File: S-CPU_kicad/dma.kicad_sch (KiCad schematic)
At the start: 115 parts

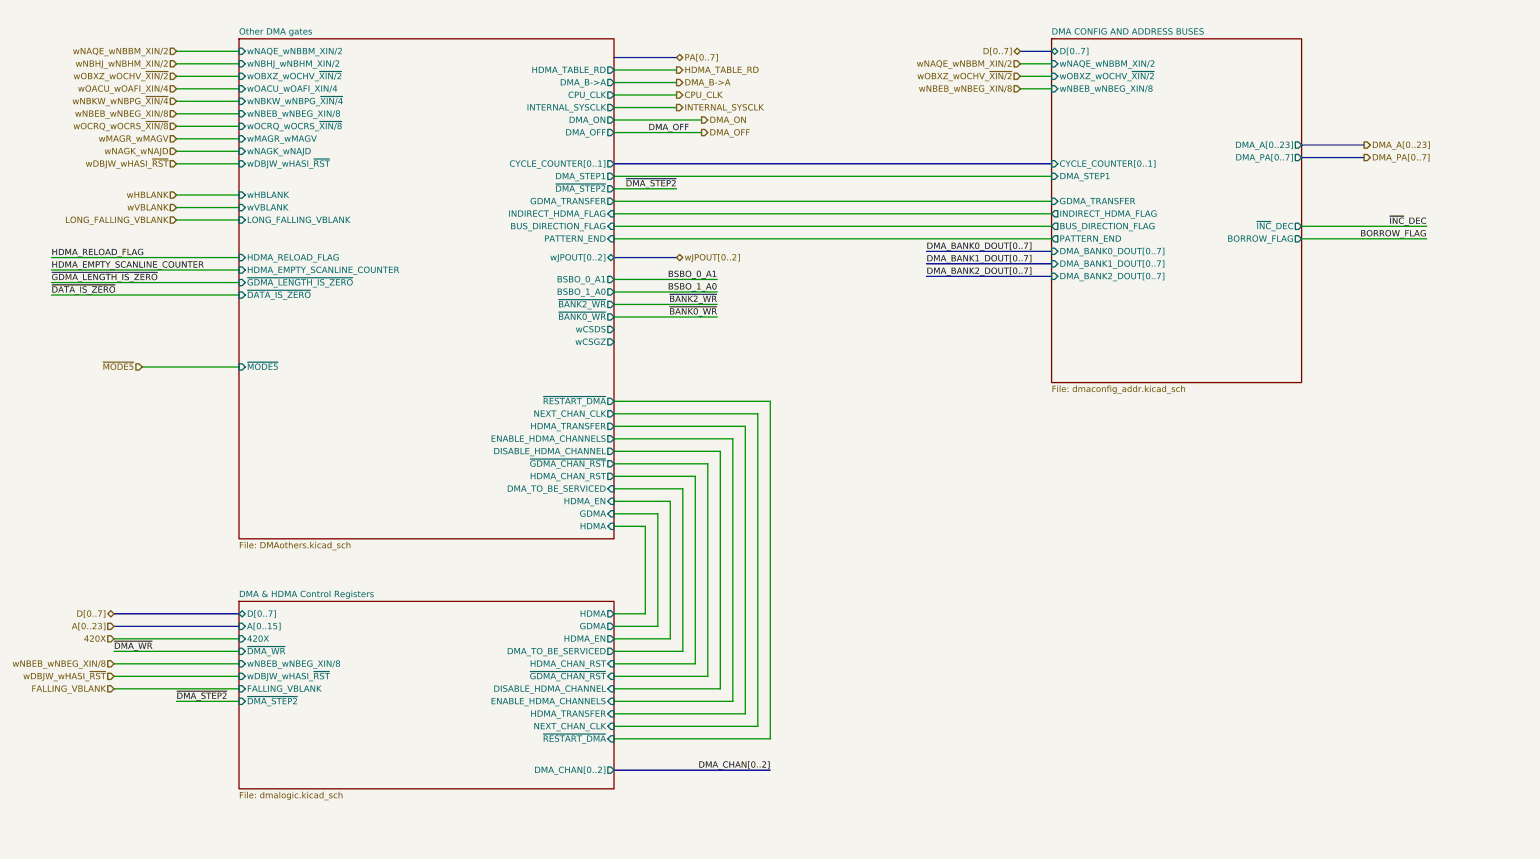
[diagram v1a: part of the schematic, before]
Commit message: Further tidying of the DMA section. New sheet added dedicated to GDMA/ HDMA Start and Stop signals.
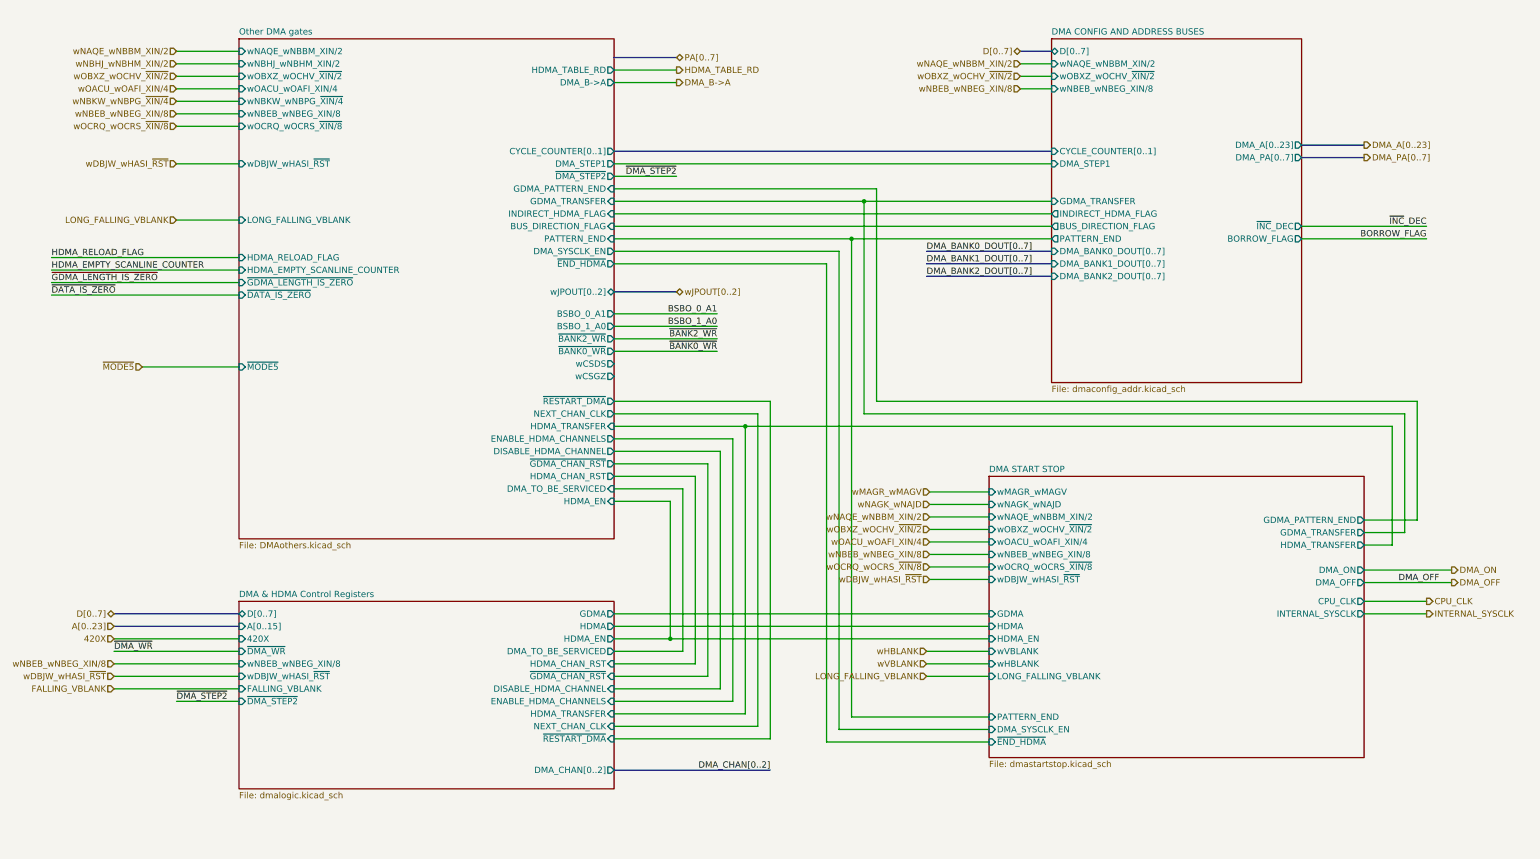
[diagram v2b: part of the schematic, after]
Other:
- added sheet DMA START STOP (dmastartstop.kicad_sch)
- sheet Other DMA gates ports: added DMA_SYSCLK_EN, GDMA_PATTERN_END, ~{END_HDMA}; removed CPU_CLK, DMA_OFF, DMA_ON, GDMA, HDMA, INTERNAL_SYSCLK, wHBLANK, wMAGR_wMAGV, wNAGK_wNAJD, wVBLANK

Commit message: General update a
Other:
- sheet DMA & HDMA Control Registers ports: added ~{DMA_CHAN_RST}; removed ~{GDMA_CHAN_RST}
- sheet DMA START STOP ports: added HDMA_ON; removed none
- sheet Other DMA gates ports: added DMA_ON, HDMA_ON, PA[0..7], ~{DMA_CHAN_RST}; removed ~{GDMA_CHAN_RST}
- note added: "DMA Registers Parameters for DMA Transfer B Address A Address (Low Byte) A Address (High Byte) A Address Bank Number Bytes to Transfer (Low Byte) (DMA) Number Bytes to Transfer (High Byte) (DMA) Data Bank (H-DMA) A2 Table Address (Low Byte) A2 Table Address (High Byte) Number of Lines to Transfer (HDMA) Fast Access memory x x x Fast Access memory mirror"
- note removed: "DMA Registers Parameters for DMA Transfer B Address A Address (Low Byte) A Address (High Byte) A Address Bank Number Bytes to Transfer (Low Byte) (DMA) Number Bytes to Transfer (High Byte) (DMA) Data Bank (H-DMA) A2 Table Address (Low Byte) A2 Table Address (High Byte) Number of Lines to Transfer (H-DMA) Fast Access memory x x x Fast Access memory mirror"
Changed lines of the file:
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@@
   (junction (at 357.505 269.24) (diameter 0) (color 0 0 0 0)
   )
+  (junction (at 783.59 273.05) (diameter 0) (color 0 0 0 0)
+  )
   (junction (at 487.045 116.84) (diameter 0) (color 0 0 0 0)
   )
@@
     (stroke (width 0) (type default))
   )
+  (wire (pts (xy 662.94 213.36) (xy 662.94 246.38))
+    (stroke (width 0) (type default))
+  )
   (wire (pts (xy 360.045 216.535) (xy 360.045 184.785))
     (stroke (width 0) (type default))
@@
     (stroke (width 0) (type default))
   )
+  (wire (pts (xy 660.4 215.9) (xy 660.4 248.92))
+    (stroke (width 0) (type default))
+  )
   (wire (pts (xy 259.08 220.98) (xy 266.065 220.98))
     (stroke (width 0) (type default))
@@
     (stroke (width 0) (type default))
   )
-  (wire (pts (xy 782.955 241.3) (xy 782.955 265.43))
+  (wire (pts (xy 788.67 241.3) (xy 788.67 265.43))
     (stroke (width 0) (type default))
   )
@@
     (stroke (width 0) (type default))
   )
+  (wire (pts (xy 781.05 248.92) (xy 781.05 270.51))
+    (stroke (width 0) (type default))
+  )
   (polyline (pts (xy 600.075 348.615) (xy 553.085 348.615))
     (stroke (width 0) (type default))
@@
     (stroke (width 0) (type default))
   )
+  (wire (pts (xy 783.59 246.38) (xy 783.59 273.05))
+    (stroke (width 0) (type default))
+  )
   (bus (pts (xy 685.8 208.28) (xy 711.2 208.28))
     (stroke (width 0) (type default))
@@
     (stroke (width 0) (type default))
   )
-  (wire (pts (xy 774.7 273.05) (xy 792.48 273.05))
-    (stroke (width 0) (type default))
-  )
   (wire (pts (xy 240.665 419.735) (xy 257.81 419.735))
     (stroke (width 0) (type default))
@@
     (stroke (width 0) (type default))
   )
-  (bus (pts (xy 622.3 216.535) (xy 635 216.535))
+  (bus (pts (xy 622.3 176.53) (xy 635 176.53))
     (stroke (width 0) (type default))
   )
@@
     (stroke (width 0) (type default))
   )
-  (wire (pts (xy 782.955 265.43) (xy 774.7 265.43))
+  (wire (pts (xy 788.67 265.43) (xy 774.7 265.43))
     (stroke (width 0) (type default))
   )
@@
     (stroke (width 0) (type default))
   )
+  (wire (pts (xy 622.3 233.68) (xy 632.46 233.68))
+    (stroke (width 0) (type default))
+  )
   (wire (pts (xy 541.655 548.005) (xy 558.165 548.005))
     (stroke (width 0) (type default))
@@
     (stroke (width 0) (type default))
   )
-  (wire (pts (xy 780.415 243.84) (xy 780.415 267.97))
+  (wire (pts (xy 786.13 243.84) (xy 786.13 267.97))
     (stroke (width 0) (type default))
   )
@@
     (stroke (width 0) (type default))
   )
+  (wire (pts (xy 774.7 273.05) (xy 783.59 273.05))
+    (stroke (width 0) (type default))
+  )
   (wire (pts (xy 156.845 422.275) (xy 227.965 422.275))
     (stroke (width 0) (type default))
@@
     (stroke (width 0) (type default))
   )
+  (wire (pts (xy 774.7 270.51) (xy 781.05 270.51))
+    (stroke (width 0) (type default))
+  )
   (wire (pts (xy 686.435 272.415) (xy 698.5 272.415))
     (stroke (width 0) (type default))
@@
     (stroke (width 0) (type default))
   )
-  (wire (pts (xy 648.97 243.84) (xy 780.415 243.84))
+  (wire (pts (xy 648.97 243.84) (xy 786.13 243.84))
     (stroke (width 0) (type default))
   )
@@
     (stroke (width 0) (type default))
   )
+  (wire (pts (xy 622.3 213.36) (xy 662.94 213.36))
+    (stroke (width 0) (type default))
+  )
   (wire (pts (xy 259.08 203.2) (xy 259.08 220.98))
     (stroke (width 0) (type default))
@@
     (stroke (width 0) (type default))
   )
-  (wire (pts (xy 785.495 262.89) (xy 774.7 262.89))
+  (wire (pts (xy 791.21 262.89) (xy 774.7 262.89))
     (stroke (width 0) (type default))
   )
@@
     (stroke (width 0) (type default))
   )
+  (wire (pts (xy 660.4 248.92) (xy 781.05 248.92))
+    (stroke (width 0) (type default))
+  )
   (wire (pts (xy 521.335 521.335) (xy 526.415 521.335))
     (stroke (width 0) (type default))
@@
     (stroke (width 0) (type default))
   )
-  (wire (pts (xy 675.64 238.76) (xy 785.495 238.76))
+  (wire (pts (xy 675.64 238.76) (xy 791.21 238.76))
     (stroke (width 0) (type default))
   )
@@
     (stroke (width 0) (type default))
   )
-  (wire (pts (xy 641.35 251.46) (xy 622.3 251.46))
+  (wire (pts (xy 622.3 251.46) (xy 641.35 251.46))
     (stroke (width 0) (type default))
   )
@@
     (stroke (width 0) (type default))
   )
-  (wire (pts (xy 780.415 267.97) (xy 774.7 267.97))
+  (wire (pts (xy 786.13 267.97) (xy 774.7 267.97))
     (stroke (width 0) (type default))
   )
@@
     (stroke (width 0) (type default))
   )
-  (wire (pts (xy 673.1 241.3) (xy 782.955 241.3))
+  (wire (pts (xy 673.1 241.3) (xy 788.67 241.3))
     (stroke (width 0) (type default))
   )
@@
     (stroke (width 0) (type default))
   )
+  (wire (pts (xy 662.94 246.38) (xy 783.59 246.38))
+    (stroke (width 0) (type default))
+  )
   (wire (pts (xy 83.82 495.3) (xy 93.345 495.3))
     (stroke (width 0) (type default))
@@
     (stroke (width 0) (type default))
   )
-  (wire (pts (xy 785.495 238.76) (xy 785.495 262.89))
+  (wire (pts (xy 791.21 238.76) (xy 791.21 262.89))
     (stroke (width 0) (type default))
   )
@@
     (stroke (width 0) (type default))
   )
+  (wire (pts (xy 783.59 273.05) (xy 792.48 273.05))
+    (stroke (width 0) (type default))
+  )
   (wire (pts (xy 261.62 289.56) (xy 266.065 289.56))
     (stroke (width 0) (type default))
@@
     (stroke (width 0) (type default))
   )
+  (wire (pts (xy 622.3 215.9) (xy 660.4 215.9))
+    (stroke (width 0) (type default))
+  )
   (wire (pts (xy 638.81 254) (xy 638.81 292.1))
     (stroke (width 0) (type default))
@@
     (stroke (width 0) (type default))
   )
+  (wire (pts (xy 632.46 231.14) (xy 622.3 231.14))
+    (stroke (width 0) (type default))
+  )
   (wire (pts (xy 362.585 445.135) (xy 356.87 445.135))
     (stroke (width 0) (type default))
@@
     (effects (font (size 1.27 1.27)) (justify left bottom))
   )
-  (text "DMA Registers\n\nParameters for DMA Transfer\nB Address\nA Address (Low Byte)\nA Address (High Byte)\nA Address Bank\nNumber Bytes to Transfer (Low Byte) (DMA)\nNumber Bytes to Transfer (High Byte) (DMA)\nData Bank (H-DMA)\nA2 Table Address (Low Byte)\nA2 Table Address (High Byte)\nNumber of Lines to Transfer (H-DMA) \nFast Access memory\nx\nx\nx\nFast Access memory mirror"
+  (text "DMA Registers\n\nParameters for DMA Transfer\nB Address\nA Address (Low Byte)\nA Address (High Byte)\nA Address Bank\nNumber Bytes to Transfer (Low Byte) (DMA)\nNumber Bytes to Transfer (High Byte) (DMA)\nData Bank (H-DMA)\nA2 Table Address (Low Byte)\nA2 Table Address (High Byte)\nNumber of Lines to Transfer (HDMA) \nFast Access memory\nx\nx\nx\nFast Access memory mirror"
     (at 554.355 387.985 0)
     (effects (font (size 1.27 1.27)) (justify left bottom))
@@
     (effects (font (size 1.27 1.27)) (justify right bottom))
   )
+  (label "wCSDS" (at 632.46 231.14 180) (fields_autoplaced)
+    (effects (font (size 1.27 1.27)) (justify right bottom))
+  )
   (label "DMA_BANK0_DOUT7" (at 237.49 205.74 0) (fields_autoplaced)
     (effects (font (size 1.27 1.27)) (justify left bottom))
@@
     (effects (font (size 1.27 1.27)) (justify right bottom))
   )
+  (label "wCSGZ" (at 632.46 233.68 180) (fields_autoplaced)
+    (effects (font (size 1.27 1.27)) (justify right bottom))
+  )
   (label "DMA_BANK0_DOUT3" (at 551.815 446.405 180) (fields_autoplaced)
     (effects (font (size 1.27 1.27)) (justify right bottom))
@@
     (effects (font (size 1.27 1.27)) (justify right))
   )
-  (hierarchical_label "wJPOUT[0..2]" (shape tri_state) (at 635 216.535 0) (fields_autoplaced)
+  (hierarchical_label "wJPOUT[0..2]" (shape tri_state) (at 635 176.53 0) (fields_autoplaced)
     (effects (font (size 1.27 1.27)) (justify left))
   )
@@
       (effects (font (size 1.27 1.27)) (justify right))
     )
-    (pin "~{GDMA_CHAN_RST}" input (at 622.3 294.64 0)
+    (pin "~{DMA_CHAN_RST}" input (at 622.3 294.64 0)
       (effects (font (size 1.27 1.27)) (justify right))
     )
@@
       (effects (font (size 1.27 1.27)) (justify right))
     )
-    (pin "~{GDMA_CHAN_RST}" output (at 622.3 251.46 0)
+    (pin "~{DMA_CHAN_RST}" output (at 622.3 251.46 0)
       (effects (font (size 1.27 1.27)) (justify right))
     )
@@
       (effects (font (size 1.27 1.27)) (justify right))
     )
-    (pin "wJPOUT[0..2]" tri_state (at 622.3 216.535 0)
+    (pin "wJPOUT[0..2]" tri_state (at 622.3 176.53 0)
       (effects (font (size 1.27 1.27)) (justify right))
     )
@@
       (effects (font (size 1.27 1.27)) (justify right))
     )
+    (pin "PA[0..7]" tri_state (at 622.3 168.91 0)
+      (effects (font (size 1.27 1.27)) (justify right))
+    )
+    (pin "DMA_ON" input (at 622.3 213.36 0)
+      (effects (font (size 1.27 1.27)) (justify right))
+    )
+    (pin "HDMA_ON" input (at 622.3 215.9 0)
+      (effects (font (size 1.27 1.27)) (justify right))
+    )
     (instances
       (project "S-CPU"
@@
       (effects (font (size 1.27 1.27)) (justify right))
     )
+    (pin "HDMA_ON" output (at 774.7 270.51 0)
+      (effects (font (size 1.27 1.27)) (justify right))
+    )

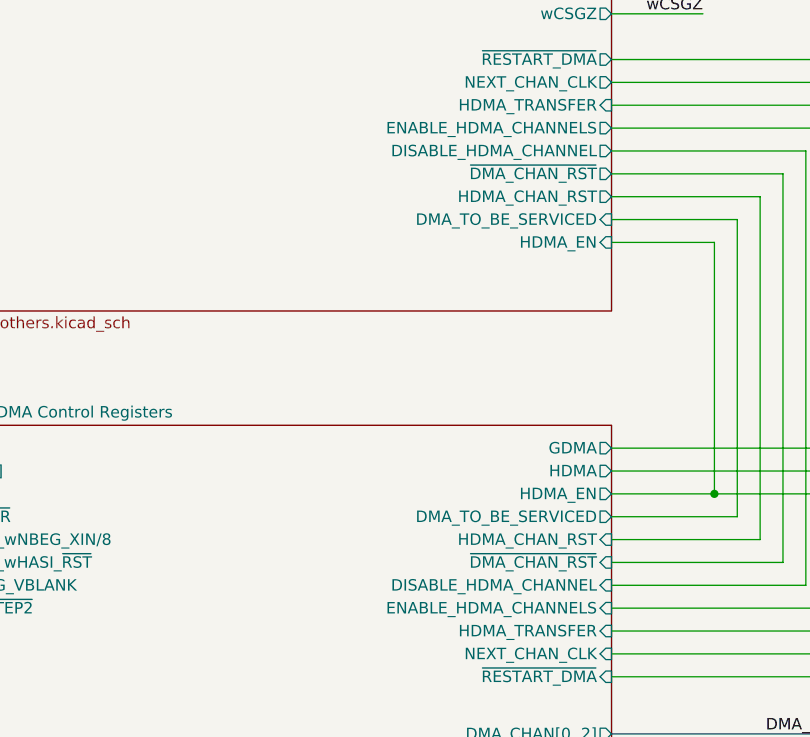
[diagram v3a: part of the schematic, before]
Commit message: HDMA section seems correct after all. More notes added.
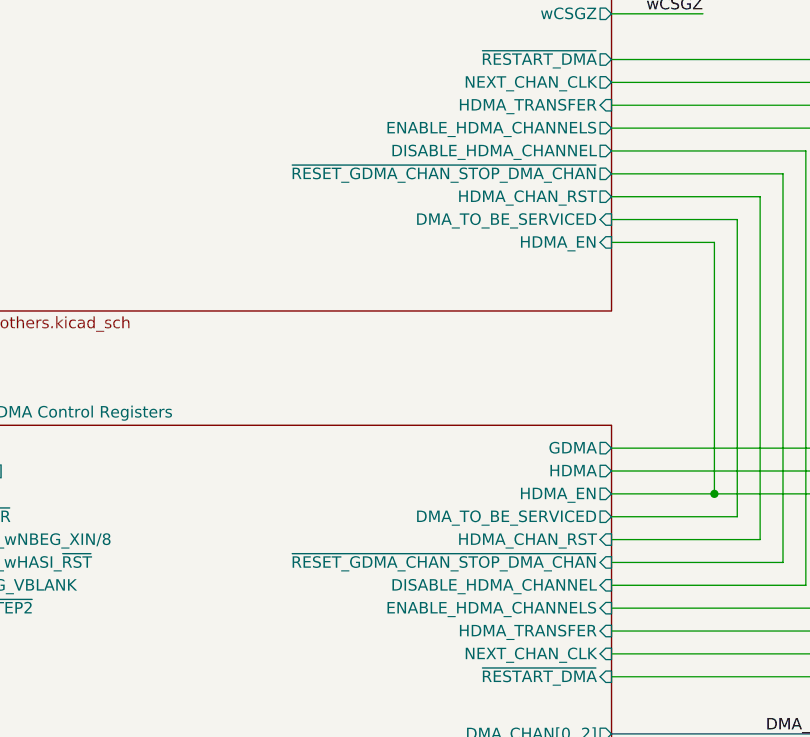
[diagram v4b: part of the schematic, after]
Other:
- sheet DMA & HDMA Control Registers ports: added ~{RESET_GDMA_CHAN_STOP_DMA_CHAN}; removed ~{DMA_CHAN_RST}
- sheet Other DMA gates ports: added ~{RESET_GDMA_CHAN_STOP_DMA_CHAN}; removed ~{DMA_CHAN_RST}
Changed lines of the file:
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@@
       (effects (font (size 1.27 1.27)) (justify right))
     )
-    (pin "~{DMA_CHAN_RST}" input (at 622.3 294.64 0)
+    (pin "~{RESET_GDMA_CHAN_STOP_DMA_CHAN}" input (at 622.3 294.64 0)
       (effects (font (size 1.27 1.27)) (justify right))
     )
@@
       (effects (font (size 1.27 1.27)) (justify right))
     )
-    (pin "~{DMA_CHAN_RST}" output (at 622.3 251.46 0)
+    (pin "~{RESET_GDMA_CHAN_STOP_DMA_CHAN}" output (at 622.3 251.46 0)
       (effects (font (size 1.27 1.27)) (justify right))
     )

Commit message: More DMA updates - extra notes regarding behaviour
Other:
- note added: "Latched on cycle 7 to 0 transition"
- note added: "Valid on cycle 0-1 and 4-5"
- moved on the sheet: OMNN
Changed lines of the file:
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@@
   (junction (at 261.62 236.22) (diameter 0) (color 0 0 0 0)
   )
+  (junction (at 351.79 512.445) (diameter 0) (color 0 0 0 0)
+  )
   (junction (at 521.335 550.545) (diameter 0) (color 0 0 0 0)
   )
@@
   (junction (at 357.505 427.99) (diameter 0) (color 0 0 0 0)
   )
-  (junction (at 351.79 531.495) (diameter 0) (color 0 0 0 0)
-  )
   (junction (at 489.585 119.38) (diameter 0) (color 0 0 0 0)
   )
@@
     (stroke (width 0) (type default))
   )
-  (wire (pts (xy 351.79 531.495) (xy 341.63 531.495))
+  (wire (pts (xy 351.79 512.445) (xy 330.2 512.445))
     (stroke (width 0) (type default))
   )
@@
     (stroke (width 0) (type default))
   )
-  (wire (pts (xy 314.325 531.495) (xy 328.93 531.495))
+  (wire (pts (xy 302.895 512.445) (xy 317.5 512.445))
     (stroke (width 0) (type default))
   )
@@
     (effects (font (size 1.27 1.27)) (justify left bottom))
   )
+  (text "Latched on cycle 7 to 0 transition" (at 324.485 454.025 0)
+    (effects (font (size 1.27 1.27)) (justify left bottom))
+  )
   (text "AMCK\nB1_ENB\n\n0\n1\n1\n1\n0\n1\n1\n0\n1\n1\n1\n0\nx\nx\nx\n0" (at 521.335 387.985 0)
     (effects (font (size 1.27 1.27)) (justify left bottom))
@@
     (effects (font (size 1.27 1.27)) (justify left bottom))
   )
+  (text "Valid on cycle 0-1 and 4-5" (at 217.17 19.685 0)
+    (effects (font (size 1.27 1.27)) (justify left bottom))
+  )
   (text "DMA RAM control signals decoding (Registers 43x0-43xF)"
     (at 495.3 342.9 0)
@@
     (effects (font (size 1.27 1.27)) (justify left bottom))
   )
+  (text "Valid on cycle 0-1 and 4-5" (at 241.935 184.15 0)
+    (effects (font (size 1.27 1.27)) (justify left bottom))
+  )
   (label "A1" (at 83.82 556.895 0) (fields_autoplaced)
     (effects (font (size 1.27 1.27)) (justify left bottom))
@@
     (effects (font (size 1.27 1.27)) (justify left bottom))
   )
-  (label "DMA_OFF" (at 314.325 531.495 0) (fields_autoplaced)
+  (label "DMA_OFF" (at 302.895 512.445 0) (fields_autoplaced)
     (effects (font (size 1.27 1.27)) (justify left bottom))
   )
@@
     )
   )
-  (symbol (lib_id "Ricoh_Cells:INVERTER_A") (at 335.28 531.495 0) (unit 1)
+  (symbol (lib_id "Ricoh_Cells:INVERTER_A") (at 323.85 512.445 0) (unit 1)
     (in_bom yes) (on_board yes) (dnp no)
-    (property "Reference" "OMNN" (at 335.28 524.6751 0)
+    (property "Reference" "OMNN" (at 323.85 505.6251 0)
       (effects (font (size 1.27 1.27)))
     )
-    (property "Value" "INVERTER_A" (at 335.28 527.05 0)
+    (property "Value" "INVERTER_A" (at 323.85 508 0)
       (effects (font (size 1.27 1.27)))
     )
-    (property "Footprint" "" (at 332.74 531.495 0)
+    (property "Footprint" "" (at 321.31 512.445 0)
       (effects (font (size 1.27 1.27)) hide)
     )
-    (property "Datasheet" "http://iceboy.a-singer.de/doc/dmg_cells.html#inv_a" (at 336.55 539.115 0)
+    (property "Datasheet" "http://iceboy.a-singer.de/doc/dmg_cells.html#inv_a" (at 325.12 520.065 0)
       (effects (font (size 1.27 1.27)) hide)
     )

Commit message: Fix ERC errors in schematics.
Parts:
- removed EMAU, EMCQ, EMGX: INVERTER_A, symbol Ricoh_Cells:INVERTER_A
- renumbered UKYL to UKVK
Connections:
- net DMA_CHAN0: now also ZKBA.15
- net DMA_CHAN1: now also ZKBA.25
- net DMA_CHAN2: now also ZKBW.5
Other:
- sheet DMA CONFIG AND ADDRESS BUSES ports: added PATTERN_COUNTER[0..1], ~{DMA_BANK0_RD}, ~{DMA_BANK1_RD}, ~{DMA_BANK2_RD}, ~{MODE5}; removed CYCLE_COUNTER[0..1]
- sheet Other DMA gates ports: added PATTERN_COUNTER[0..1]; removed CYCLE_COUNTER[0..1]
- title: SNES S-CPU Schematics  -> Reverse Engineered SNES S-CPU Schematics 
